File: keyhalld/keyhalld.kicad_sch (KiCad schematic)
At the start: 14 parts, among them J1 Conn_01x06_Pin, U1 RP2350A, U2 CD74HC4067M, Y1 12MHz

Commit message: Schematic done for Motherboard
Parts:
- added D1: WS2812B-2020, LED_SMD:LED_WS2812B-2020_PLCC4_2.0x2.0mm, symbol LED:WS2812B-2020
- added J2: Conn_01x04_Pin, Connector_Wire:SolderWire-0.127sqmm_1x04_P3.7mm_D0.48mm_OD1mm, symbol Connector:Conn_01x04_Pin
- added R10: 4.7k, Resistor_SMD:R_0603_1608Metric_Pad0.98x0.95mm_HandSolder, symbol Device:R
- added SW19: USB_BOOT, Button_Switch_SMD:SW_Tactile_SPST_NO_Straight_CK_PTS636Sx25SMTRLFS, symbol Switch:SW_Push
- added SW20: RESET, Button_Switch_SMD:SW_Tactile_SPST_NO_Straight_CK_PTS636Sx25SMTRLFS, symbol Switch:SW_Push
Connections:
- net GND: now also U1.59 (QSPI_SD1), D1.2 (VSS), J2.4 (Pin_4), SW19.2, SW20.2
- net RUN: now also SW20.1
- net WS2812_TX: now reaches U1.10 (GPIO7)
- net WS2812_TX: now also D1.3 (DIN)
- net USB_BOOT: now reaches U1.60 (QSPI_~{SS})
- net USB_BOOT: now also R10.2
- net MAG_UART_TX: now reaches U1.7 (GPIO4)
- net MAG_UART_TX: now also J2.3 (Pin_3)
- net MAG_UART_RX: now reaches U1.8 (GPIO5)
- net MAG_UART_RX: now also J2.2 (Pin_2)
- new net: R10.1, SW19.1
- new net +5V: D1.4 (VDD), J2.1 (Pin_1)
- no-connect marks 28 -> 24
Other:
- note added: "BigMagSafe"
- note added: "Reset"
- note added: "Status LED"
- note added: "USB Boot"
- note removed: "TODO MagSafe 4 Pin UART Connector header/pins"

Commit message: Schematic is approved. High quality content
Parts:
- J1: footprint Connector_PinHeader_1.00mm:PinHeader_1x06_P1.00mm_Vertical -> Connector_PinHeader_2.54mm:PinHeader_1x06_P2.54mm_Horizontal
- J2: footprint Connector_Wire:SolderWire-0.127sqmm_1x04_P3.7mm_D0.48mm_OD1mm -> Connector_PinHeader_2.54mm:PinHeader_1x04_P2.54mm_Vertical
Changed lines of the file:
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@@
 			)
 		)
-		(property "Footprint" "Connector_PinHeader_1.00mm:PinHeader_1x06_P1.00mm_Vertical"
+		(property "Footprint" "Connector_PinHeader_2.54mm:PinHeader_1x06_P2.54mm_Horizontal"
 			(at 24.13 73.66 0)
 			(hide yes)
@@
 			)
 		)
-		(property "Footprint" "Connector_Wire:SolderWire-0.127sqmm_1x04_P3.7mm_D0.48mm_OD1mm"
+		(property "Footprint" "Connector_PinHeader_2.54mm:PinHeader_1x04_P2.54mm_Vertical"
 			(at 25.4 147.32 0)
 			(hide yes)

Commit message: Started PCB Implementation
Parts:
- added C6: 100n, Capacitor_SMD:C_0603_1608Metric_Pad1.08x0.95mm_HandSolder, symbol Device:C
- added H1, H2, H3, H4, H5, H6, H7, H8: MP, MountingHole:MountingHole_3.2mm_M3_Pad, symbol Mechanical:MountingHole_Pad
- renumbered C3 to C1, C4 to C2, C37 to C3, C1 to C4, C2 to C5, R9 to R1, R4 to R2, R5 to R3, R1 to R4, R10 to R5, SW20 to SW1, SW19 to SW2
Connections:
- net +5V: now also C6.1
- net DBG_TX: now also U1.16 (GPIO12); no longer U1.2 (GPIO0)
- net GND: now also C6.2, H1.1, H2.1, H3.1, H4.1, H5.1, H6.1, H7.1, H8.1
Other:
- note added: "Mounting Holes"

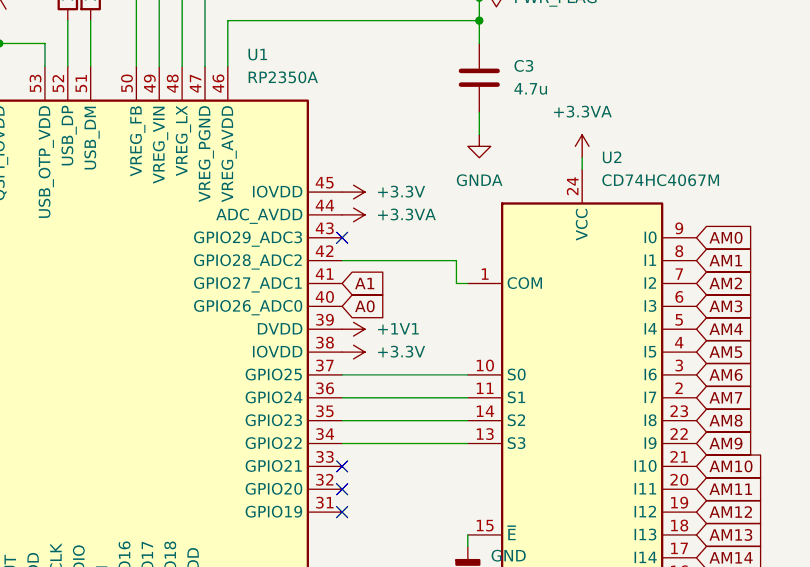
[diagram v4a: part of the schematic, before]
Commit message: ADC Pinout update
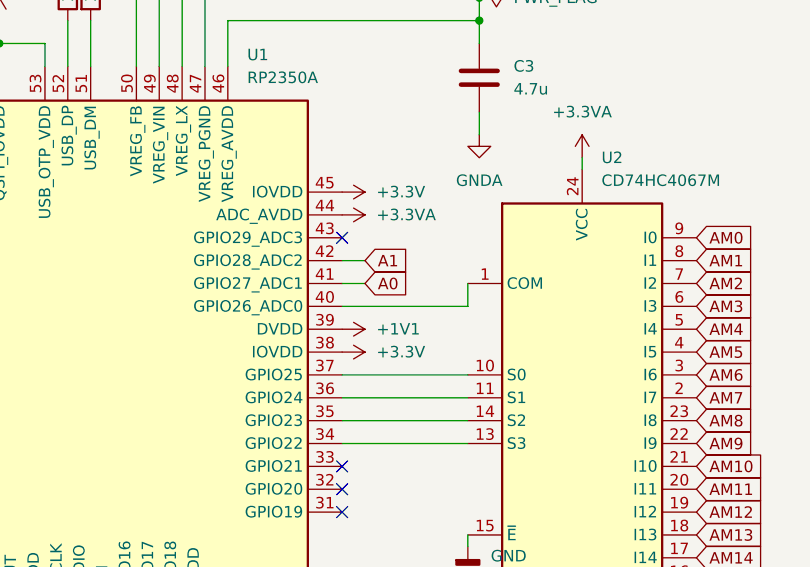
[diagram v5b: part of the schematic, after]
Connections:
- net A0: now also U1.41 (GPIO27_ADC1); no longer U1.40 (GPIO26_ADC0)
- net A1: now also U1.42 (GPIO28_ADC2); no longer U1.41 (GPIO27_ADC1)
- net at U2.1 (COM): now also U1.40 (GPIO26_ADC0); no longer U1.42 (GPIO28_ADC2)
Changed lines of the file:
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@@
-	(wire
-		(pts
-			(xy 166.37 88.9) (xy 179.07 88.9)
-		)
-		(stroke
-			(width 0)
-			(type default)
-		)
-	)
 	(wire
 		(pts
@@
 	(wire
 		(pts
+			(xy 168.91 91.44) (xy 166.37 91.44)
+		)
+		(stroke
+			(width 0)
+			(type default)
+		)
+	)
+	(wire
+		(pts
 			(xy 30.48 102.87) (xy 43.18 102.87)
 		)
@@
 	(wire
 		(pts
+			(xy 180.34 93.98) (xy 166.37 93.98)
+		)
+		(stroke
+			(width 0)
+			(type default)
+		)
+	)
+	(wire
+		(pts
 			(xy 30.48 115.57) (xy 34.29 115.57)
 		)
@@
 	(wire
 		(pts
-			(xy 179.07 91.44) (xy 179.07 88.9)
-		)
-		(stroke
-			(width 0)
-			(type default)
-		)
-	)
-	(wire
-		(pts
 			(xy 116.84 54.61) (xy 113.03 54.61)
 		)
@@
 	(wire
 		(pts
-			(xy 180.34 91.44) (xy 179.07 91.44)
-		)
-		(stroke
-			(width 0)
-			(type default)
-		)
-	)
-	(wire
-		(pts
 			(xy 170.18 35.56) (xy 170.18 38.1)
 		)
@@
 	(wire
 		(pts
+			(xy 168.91 88.9) (xy 166.37 88.9)
+		)
+		(stroke
+			(width 0)
+			(type default)
+		)
+	)
+	(wire
+		(pts
 			(xy 151.13 55.88) (xy 160.02 55.88)
 		)
@@
 		(pts
 			(xy 148.59 53.34) (xy 148.59 67.31)
+		)
+		(stroke
+			(width 0)
+			(type default)
+		)
+	)
+	(wire
+		(pts
+			(xy 180.34 91.44) (xy 180.34 93.98)
 		)
 		(stroke
@@
 	(global_label "A1"
 		(shape input)
-		(at 166.37 91.44 0)
-		(fields_autoplaced yes)
-		(effects
-			(font
-				(size 1.27 1.27)
-			)
-			(justify left)
-		)
-		(property "Intersheetrefs" "${INTERSHEET_REFS}"
-			(at 171.6533 91.44 0)
+		(at 168.91 88.9 0)
+		(fields_autoplaced yes)
+		(effects
+			(font
+				(size 1.27 1.27)
+			)
+			(justify left)
+		)
+		(property "Intersheetrefs" "${INTERSHEET_REFS}"
+			(at 174.1933 88.9 0)
 			(hide yes)
 			(show_name no)
@@
 	(global_label "A0"
 		(shape input)
-		(at 166.37 93.98 0)
-		(fields_autoplaced yes)
-		(effects
-			(font
-				(size 1.27 1.27)
-			)
-			(justify left)
-		)
-		(property "Intersheetrefs" "${INTERSHEET_REFS}"
-			(at 171.6533 93.98 0)
-			(hide yes)
-			(show_name no)
+		(at 168.91 91.44 0)
+		(fields_autoplaced yes)
+		(effects
+			(font
+				(size 1.27 1.27)
+			)
+			(justify left)
+		)
+		(property "Intersheetrefs" "${INTERSHEET_REFS}"
+			(at 174.1933 91.44 0)
+			(hide yes)
+			(show_name no)

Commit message: Store WIP results
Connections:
- net SWCLK: now also J1.3 (Pin_3); no longer J1.2 (Pin_2)
- net SWDIO: now also J1.2 (Pin_2); no longer J1.3 (Pin_3)

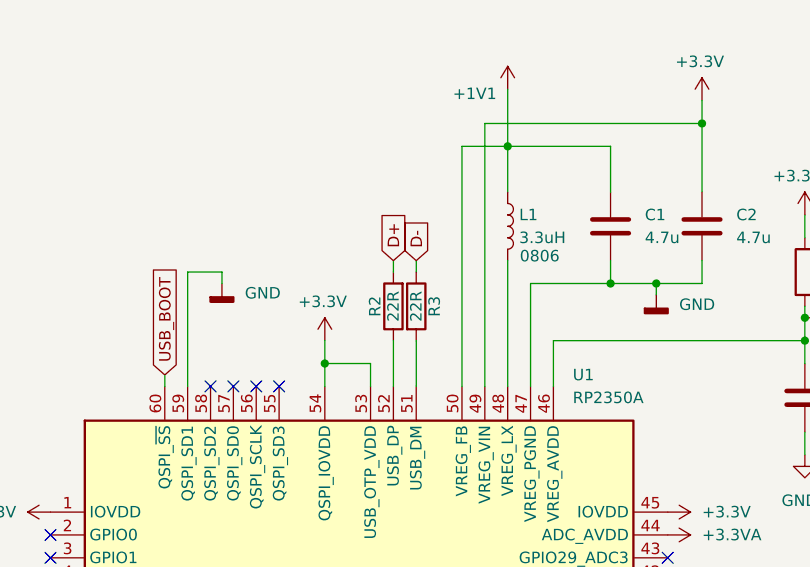
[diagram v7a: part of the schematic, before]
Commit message: route usb and ldo
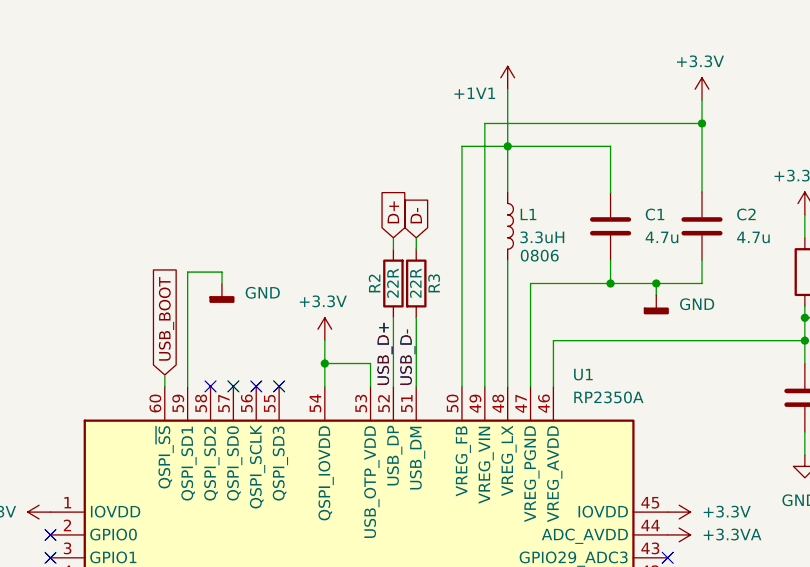
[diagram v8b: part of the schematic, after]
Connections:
- net USB_D-: now reaches R3.2, U1.51 (USB_DM)
- net USB_D+: now reaches R2.1, U1.52 (USB_DP)
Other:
- moved on the sheet: R2, R3
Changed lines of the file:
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@@
 	(wire
 		(pts
-			(xy 135.89 53.34) (xy 135.89 54.61)
+			(xy 135.89 50.8) (xy 135.89 52.07)
 		)
 		(stroke
@@
 	(wire
 		(pts
-			(xy 135.89 62.23) (xy 135.89 67.31)
+			(xy 135.89 59.69) (xy 135.89 67.31)
 		)
 		(stroke
@@
 	(wire
 		(pts
-			(xy 138.43 53.34) (xy 138.43 54.61)
+			(xy 138.43 50.8) (xy 138.43 52.07)
 		)
 		(stroke
@@
 	(wire
 		(pts
-			(xy 138.43 62.23) (xy 138.43 67.31)
+			(xy 138.43 59.69) (xy 138.43 67.31)
 		)
 		(stroke
@@
 		)
 	)
+	(label "USB_D+"
+		(at 135.89 67.31 90)
+		(effects
+			(font
+				(size 1.27 1.27)
+			)
+			(justify left bottom)
+		)
+	)
+	(label "USB_D-"
+		(at 138.43 67.31 90)
+		(effects
+			(font
+				(size 1.27 1.27)
+			)
+			(justify left bottom)
+		)
+	)
 	(global_label "AM7"
 		(shape input)
@@
 	(global_label "D+"
 		(shape input)
-		(at 135.89 53.34 90)
+		(at 135.89 50.8 90)
 		(fields_autoplaced yes)
 		(effects
@@
 		)
 		(property "Intersheetrefs" "${INTERSHEET_REFS}"
-			(at 135.89 47.5124 90)
+			(at 135.89 44.9724 90)
 			(hide yes)
 			(show_name no)
@@
 	(global_label "D-"
 		(shape input)
-		(at 138.43 53.34 90)
+		(at 138.43 50.8 90)
 		(fields_autoplaced yes)
 		(effects
@@
 		)
 		(property "Intersheetrefs" "${INTERSHEET_REFS}"
-			(at 138.43 47.5124 90)
+			(at 138.43 44.9724 90)
 			(hide yes)
 			(show_name no)
@@
 	(symbol
 		(lib_id "Device:R")
-		(at 138.43 58.42 0)
+		(at 138.43 55.88 0)
 		(unit 1)
 		(body_style 1)
@@
 		(dnp no)
 		(property "Reference" "R3"
-			(at 140.462 58.42 90)
+			(at 140.462 55.88 90)
 			(show_name no)
 			(do_not_autoplace no)
@@
 		)
 		(property "Value" "22R"
-			(at 138.43 58.42 90)
+			(at 138.43 55.88 90)
 			(show_name no)
 			(do_not_autoplace no)
@@
 		)
 		(property "Footprint" "Resistor_SMD:R_0603_1608Metric_Pad0.98x0.95mm_HandSolder"
-			(at 136.652 58.42 90)
+			(at 136.652 55.88 90)
 			(hide yes)
 			(show_name no)
@@
 		)
 		(property "Datasheet" ""
-			(at 138.43 58.42 0)
+			(at 138.43 55.88 0)
 			(hide yes)
 			(show_name no)
@@
 		)
 		(property "Description" "Resistor"
-			(at 138.43 58.42 0)
+			(at 138.43 55.88 0)
 			(hide yes)
 			(show_name no)
@@
 	(symbol
 		(lib_id "Device:R")
-		(at 135.89 58.42 180)
+		(at 135.89 55.88 180)
 		(unit 1)
 		(body_style 1)
@@
 		(dnp no)
 		(property "Reference" "R2"
-			(at 133.858 58.42 90)
+			(at 133.858 55.88 90)
 			(show_name no)
 			(do_not_autoplace no)
@@
 		)
 		(property "Value" "22R"
-			(at 135.89 58.42 90)
+			(at 135.89 55.88 90)
 			(show_name no)
 			(do_not_autoplace no)
@@
 		)
 		(property "Footprint" "Resistor_SMD:R_0603_1608Metric_Pad0.98x0.95mm_HandSolder"
-			(at 137.668 58.42 90)
+			(at 137.668 55.88 90)
 			(hide yes)
 			(show_name no)
@@
 		)
 		(property "Datasheet" ""
-			(at 135.89 58.42 0)
+			(at 135.89 55.88 0)
 			(hide yes)
 			(show_name no)
@@
 		)
 		(property "Description" "Resistor"
-			(at 135.89 58.42 0)
+			(at 135.89 55.88 0)
 			(hide yes)
 			(show_name no)
